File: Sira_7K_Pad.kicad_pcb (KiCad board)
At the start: 2 copper layers, 136.5 x 85.7 mm, 30 parts, among them J1 AVR-ISP-6, SW1 SW_Push, U1 ATmega32U4-A, U2 PRTR5V0U2X, Y1 Crystal_GND24_Small

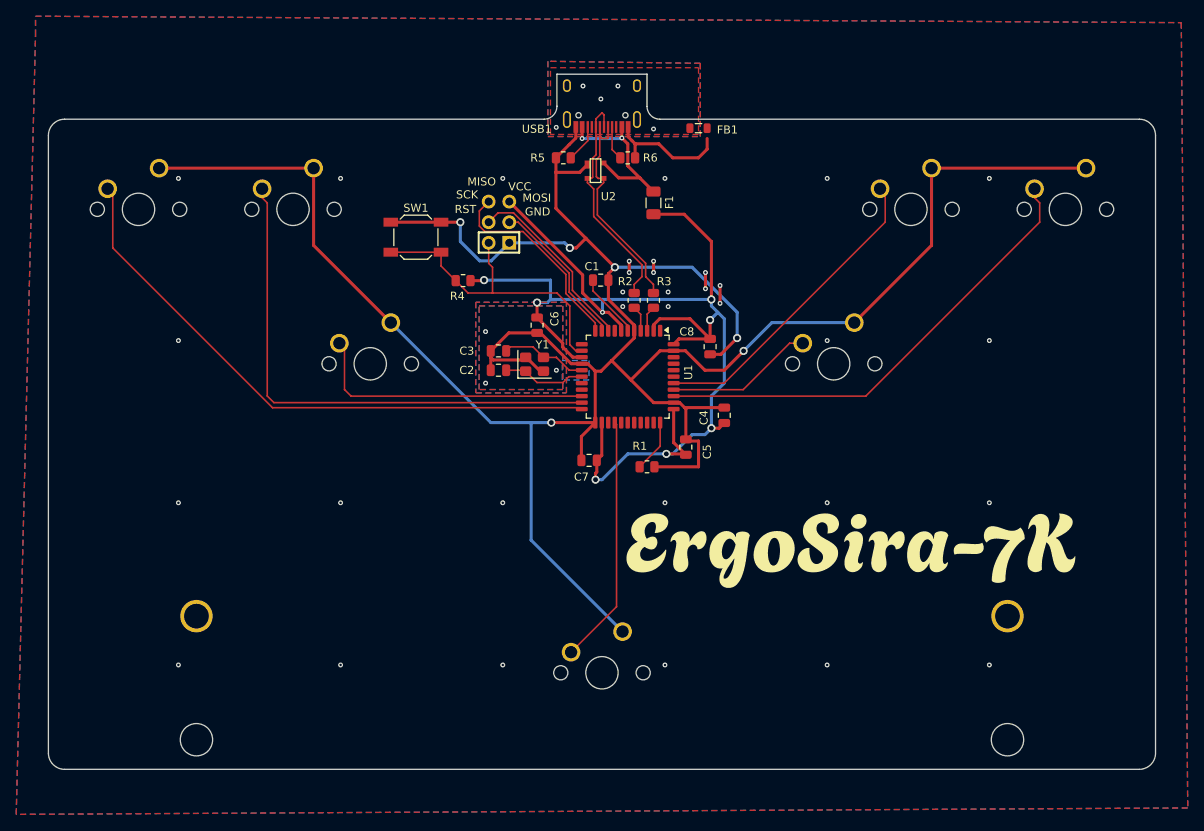
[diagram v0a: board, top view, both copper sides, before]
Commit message: Fixed incorrect decoupling capacitors routing
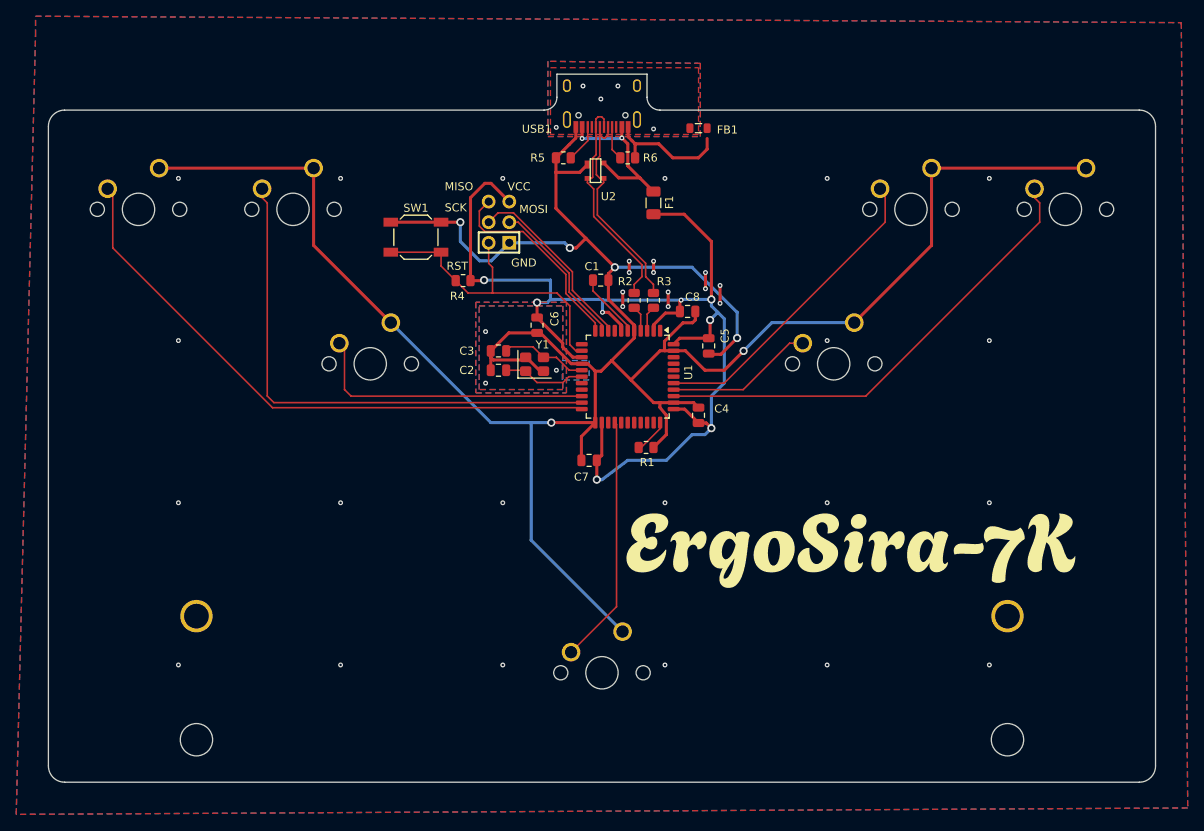
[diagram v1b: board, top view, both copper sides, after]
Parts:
- moved C5 12.8 mm to (160.8, 92.2), turned to -90 degrees
- moved C8 5.15 mm to (158.2, 88.0), turned to 0 degrees
- moved C4 3.18 mm to (159.5, 100.8)
- moved R1 2.38 mm to (153.1, 104.8)
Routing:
- net +5V: track 152.5 -> 142.5 mm
- net Net-(U1-~{HWB}/PE2): track 6.50 -> 4.35 mm
- net DP: track 28.7 -> 27.9 mm
- net DN: track 28.3 -> 27.7 mm
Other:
- board size 136.5 x 85.7 mm -> 136.5 x 87.3 mm

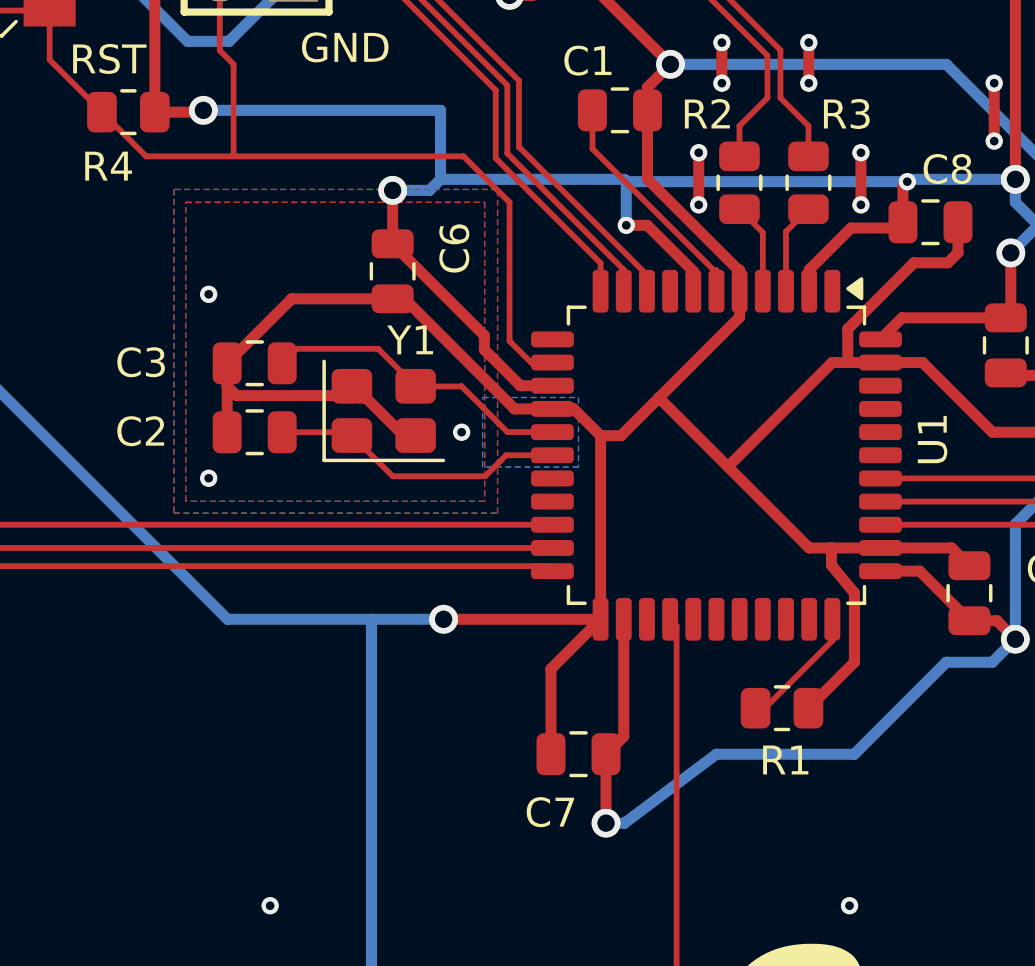
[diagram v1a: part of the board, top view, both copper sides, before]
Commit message: Moved decoupling capacitor outside of crystal ground zone
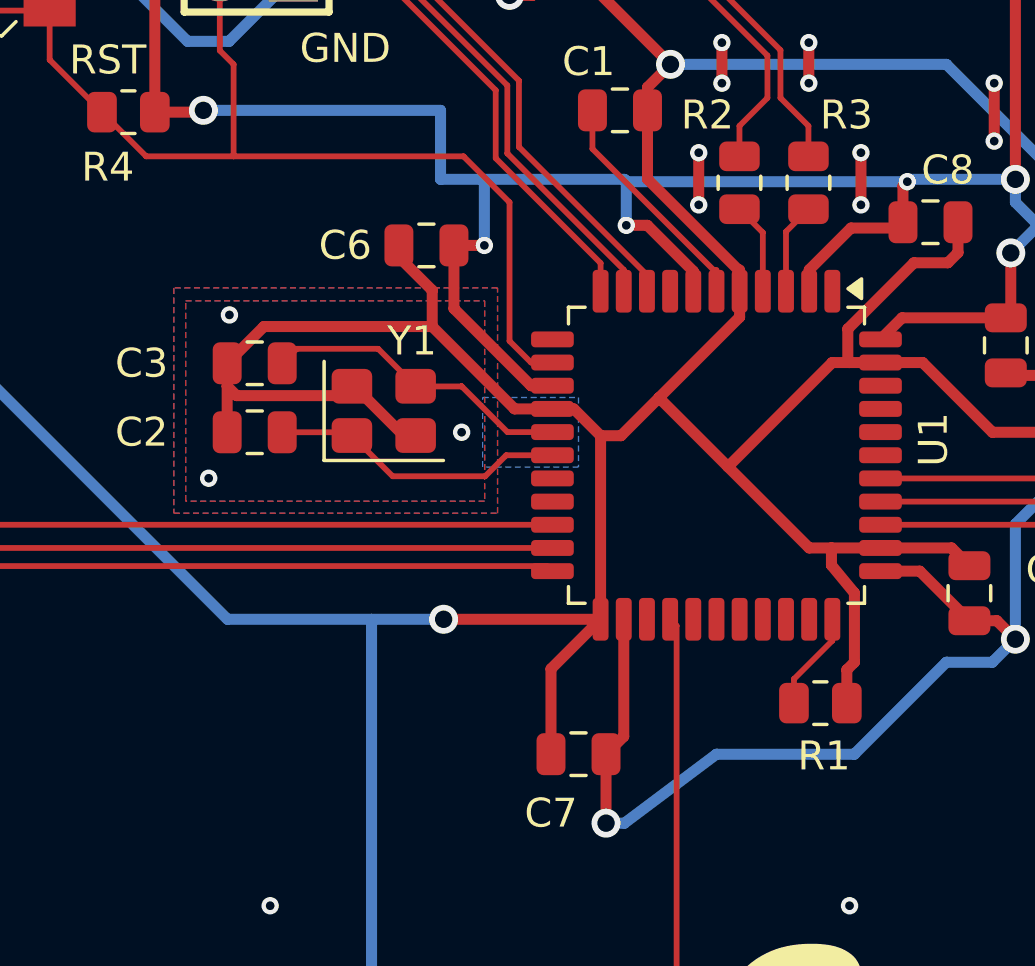
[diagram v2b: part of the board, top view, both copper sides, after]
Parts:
- moved C6 1.47 mm to (140.8, 88.8), turned to 180 degrees
- moved R1 1.34 mm to (154.4, 104.6)
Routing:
- net GND: track 363.4 -> 365.1 mm
- net +5V: track 142.5 -> 141.0 mm
- net Net-(U1-~{HWB}/PE2): track 4.35 -> 3.44 mm

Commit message: cleanup
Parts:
- moved R6 1.31 mm to (152.0, 69.6)
- moved C6 0.60 mm to (140.2, 88.8)
- moved C1 0.26 mm to (147.5, 84.4)
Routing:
- net GND: track 365.1 -> 358.8 mm, vias 42 -> 34
- net +5V: track 141.0 -> 143.9 mm
- net Net-(USB1-CC1): track 4.22 -> 5.64 mm
- net VCC: track 21.2 -> 22.0 mm

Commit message: cleanup
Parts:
- moved F1 2.07 mm to (152.0, 75.2)
- moved U2 1.76 mm to (146.8, 72.4)
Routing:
- net VCC: track 22.0 -> 20.8 mm
- net +5V: track 143.9 -> 143.2 mm
- net GND: track 358.8 -> 358.4 mm, vias 34 -> 38
